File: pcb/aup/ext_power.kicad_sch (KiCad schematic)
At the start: 27 parts, among them Q1 AO3401A, Q2 AO3401A, U2 USBLC6-2SC6, U3 TPS563257DRLR

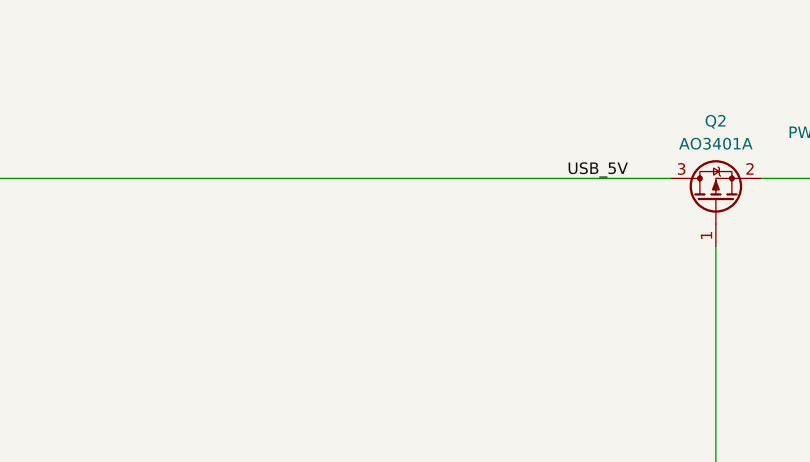
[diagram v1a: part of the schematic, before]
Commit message: Add some todo's on schematic. Add vias to fpga
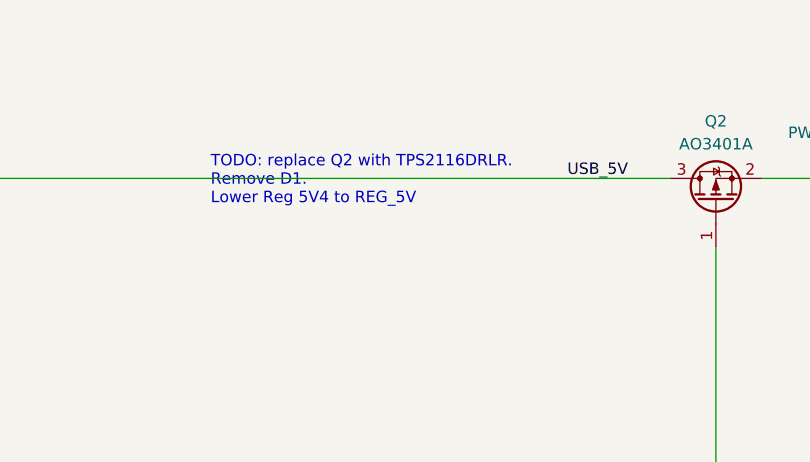
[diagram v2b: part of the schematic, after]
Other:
- note added: "TODO: replace Q2 with TPS2116DRLR. Remove D1. Lower Reg 5V4 to REG_5V"
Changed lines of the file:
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@@
 		(title "External Power")
+	)
+	(text "TODO: replace Q2 with TPS2116DRLR.\nRemove D1.\nLower Reg 5V4 to REG_5V"
+		(exclude_from_sim no)
+		(at 172.466 45.974 0)
+		(effects
+			(font
+				(size 1.27 1.27)
+			)
+			(justify left)
+		)
 	)
 	(text "The 12 to 5V regulator outputs 5.4V, with the expectation that it drops after \nthe Schottky by 0.3v under light load, and 0.5v under heavy load. (i.e. 4.9 to 5.1 final\nvoltages) This is based on the VF curves in the SS34 datasheet.\n\nR values based on availability of JLCPCB basic parts. The voltage divider for FB uses \nthe series resistors in the top portion since this seemed to be the only way to achieve\nthe desired ratio with basic parts."

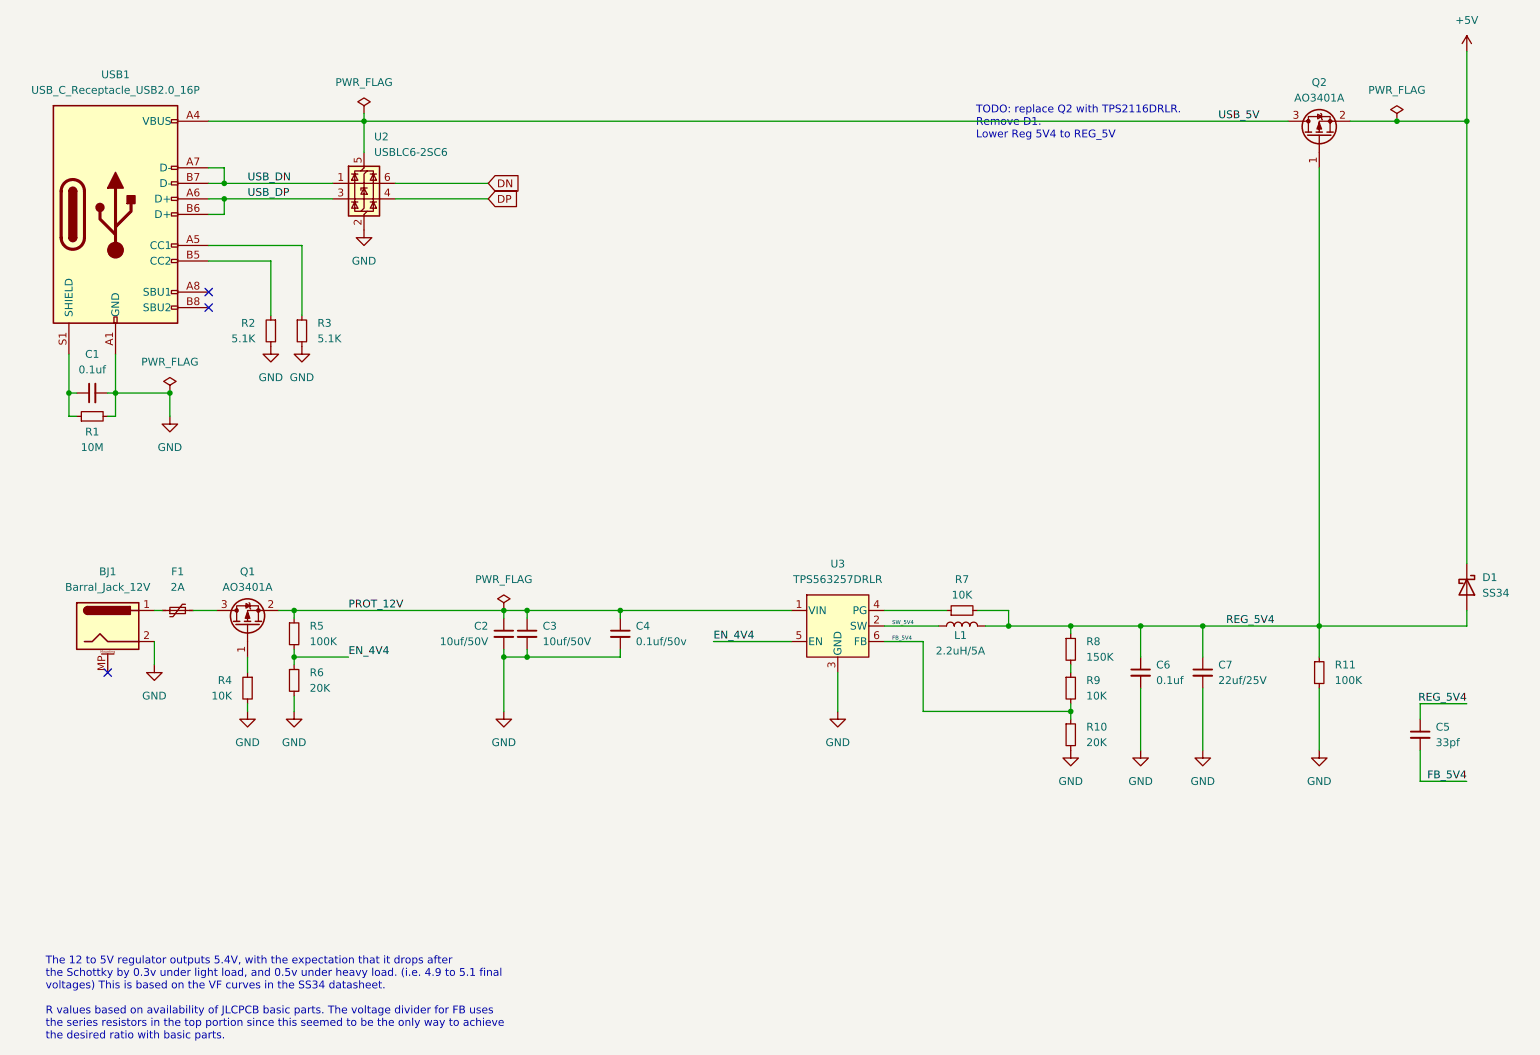
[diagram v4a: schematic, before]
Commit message: Use TPS2116DRLR for Vin mux
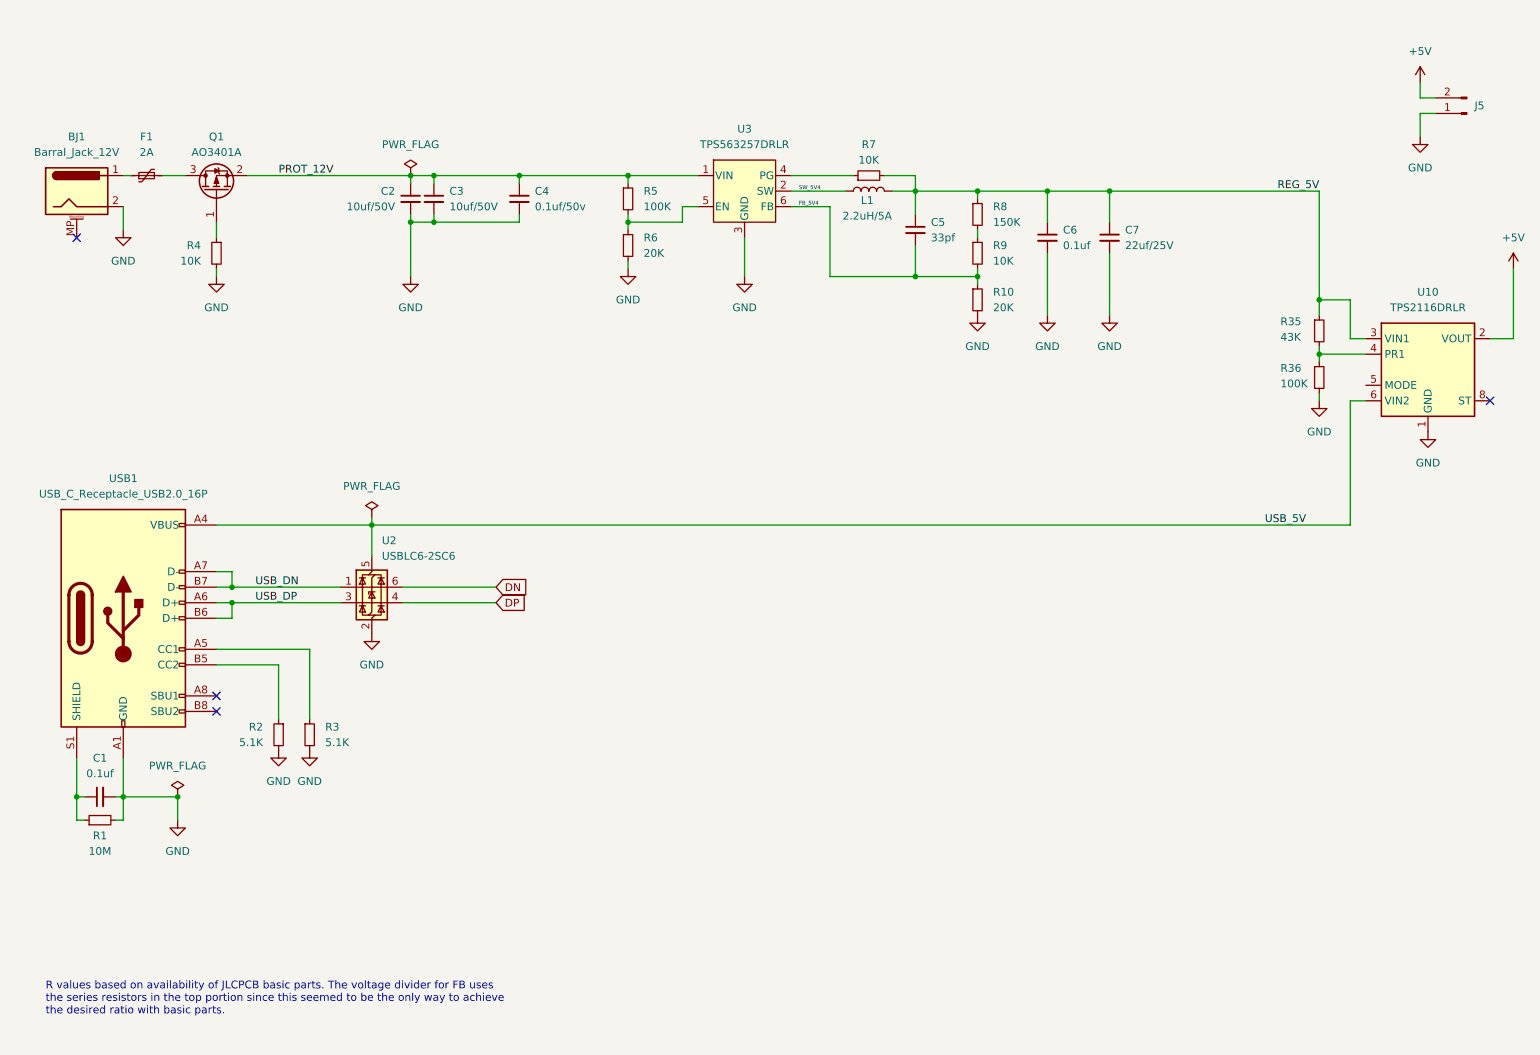
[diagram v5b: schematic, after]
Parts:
- removed D1: SS34, Diode_SMD:D_SMA, symbol !Misc:SS34
- removed Q2: AO3401A, Package_TO_SOT_SMD:SOT-23, symbol !Misc:AO3401A
- removed R11: 100K, Resistor_SMD:R_0603_1608Metric, symbol !Misc:R_100K_0603
- added J5: Conn_01x02_Pin, symbol Connector:Conn_01x02_Pin
- added R35: 43K, Resistor_SMD:R_0603_1608Metric, symbol !Misc:R_43K_0603
- added R36: 100K, Resistor_SMD:R_0603_1608Metric, symbol !Misc:R_100K_0603
- added U10: TPS2116DRLR, Package_TO_SOT_SMD:SOT-583-8, symbol !Misc:TPS2116DRLR
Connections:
- net +5V: now also J5.2 (Pin_2), U10.2 (VOUT), U10.7 (VOUT)
- net GND: now also J5.1 (Pin_1), R36.2, U10.1 (GND)
- net USB_5V: now also U10.6 (VIN2)
- net EN_4V4: no longer names the net of R5.2, R6.1, U3.5 (EN)
- net REG_5V4 renamed REG_5V
- net REG_5V: now also R35.1, U10.3 (VIN1)
- new net: R35.2, R36.1, U10.4 (PR1)
- no-connect marks 3 -> 4
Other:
- note added: "R values based on availability of JLCPCB basic parts. The voltage divider for FB uses the series resistors in the top portion since this seemed to be the only way to achieve the desired ratio with basic parts."
- note removed: "TODO: replace Q2 with TPS2116DRLR. Remove D1. Lower Reg 5V4 to REG_5V"
- note removed: "The 12 to 5V regulator outputs 5.4V, with the expectation that it drops after the Schottky by 0.3v under light load, and 0.5v under heavy load. (i.e. 4.9 to 5.1 final voltages) This is based on the VF curves in the SS34 datasheet. R values based on availability of JLCPCB basic parts. The voltage divider for FB uses the series resistors in the top portion since this seemed to be the only way to ac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"
- moved on the sheet: BJ1, C1, C2, C3, C4, C5, C6, C7, F1, L1, Q1, R1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

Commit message: Start of regulator rework
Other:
- moved on the sheet: U2
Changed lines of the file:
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@@
 	)
 	(junction
-		(at 73.66 111.76)
+		(at 80.01 111.76)
 		(diameter 0)
 		(color 0 0 0 0)
@@
 	(wire
 		(pts
-			(xy 73.66 111.76) (xy 73.66 116.84)
+			(xy 80.01 111.76) (xy 80.01 116.84)
 		)
 		(stroke
@@
 	(wire
 		(pts
-			(xy 48.26 111.76) (xy 73.66 111.76)
+			(xy 48.26 111.76) (xy 80.01 111.76)
 		)
 		(stroke
@@
 	(wire
 		(pts
-			(xy 73.66 111.76) (xy 73.66 110.49)
+			(xy 80.01 111.76) (xy 80.01 110.49)
 		)
 		(stroke
@@
 	(wire
 		(pts
-			(xy 50.8 124.46) (xy 68.58 124.46)
+			(xy 50.8 124.46) (xy 74.93 124.46)
 		)
 		(stroke
@@
 	(wire
 		(pts
-			(xy 78.74 124.46) (xy 93.98 124.46)
+			(xy 85.09 124.46) (xy 100.33 124.46)
 		)
 		(stroke
@@
 	(wire
 		(pts
-			(xy 50.8 121.92) (xy 68.58 121.92)
+			(xy 50.8 121.92) (xy 74.93 121.92)
 		)
 		(stroke
@@
 	(wire
 		(pts
+			(xy 80.01 111.76) (xy 233.68 111.76)
+		)
+		(stroke
+			(width 0)
+			(type default)
+		)
+	)
+	(wire
+		(pts
 			(xy 247.65 44.45) (xy 245.11 44.45)
 		)
@@
 	(wire
 		(pts
-			(xy 73.66 111.76) (xy 233.68 111.76)
-		)
-		(stroke
-			(width 0)
-			(type default)
-		)
-	)
-	(wire
-		(pts
 			(xy 31.75 156.21) (xy 33.02 156.21)
 		)
@@
 	(wire
 		(pts
-			(xy 78.74 121.92) (xy 93.98 121.92)
+			(xy 85.09 121.92) (xy 100.33 121.92)
 		)
 		(stroke
@@
 	(global_label "DP"
 		(shape input)
-		(at 93.98 124.46 0)
+		(at 100.33 124.46 0)
 		(fields_autoplaced yes)
 		(effects
@@
 		)
 		(property "Intersheetrefs" "${INTERSHEET_REFS}"
-			(at 99.5052 124.46 0)
+			(at 105.8552 124.46 0)
 			(effects
 				(font
@@
 	(global_label "DN"
 		(shape input)
-		(at 93.98 121.92 0)
+		(at 100.33 121.92 0)
 		(fields_autoplaced yes)
 		(effects
@@
 		)
 		(property "Intersheetrefs" "${INTERSHEET_REFS}"
-			(at 99.5657 121.92 0)
+			(at 105.9157 121.92 0)
 			(effects
 				(font
@@
 	(symbol
 		(lib_id "power:GND")
-		(at 73.66 129.54 0)
+		(at 80.01 129.54 0)
 		(unit 1)
 		(exclude_from_sim no)
@@
 		(fields_autoplaced yes)
 		(property "Reference" "#PWR06"
-			(at 73.66 135.89 0)
+			(at 80.01 135.89 0)
 			(effects
 				(font
@@
 		)
 		(property "Value" "GND"
-			(at 73.66 134.62 0)
+			(at 80.01 134.62 0)
 			(effects
 				(font
@@
 		)
 		(property "Footprint" ""
-			(at 73.66 129.54 0)
+			(at 80.01 129.54 0)
 			(effects
 				(font
@@
 		)
 		(property "Datasheet" ""
-			(at 73.66 129.54 0)
+			(at 80.01 129.54 0)
 			(effects
 				(font
@@
 		)
 		(property "Description" "Power symbol creates a global label with name \"GND\" , ground"
-			(at 73.66 129.54 0)
+			(at 80.01 129.54 0)
 			(effects
 				(font
@@
 	(symbol
 		(lib_id "!Misc:USBLC6-2SC6")
-		(at 73.66 121.92 0)
+		(at 80.01 121.92 0)
 		(unit 1)
 		(exclude_from_sim no)
@@
 		(fields_autoplaced yes)
 		(property "Reference" "U2"
-			(at 75.3111 114.3 0)
+			(at 81.6611 114.3 0)
 			(effects
 				(font
@@
 		)
 		(property "Value" "USBLC6-2SC6"
-			(at 75.3111 116.84 0)
+			(at 81.6611 116.84 0)
 			(effects
 				(font
@@
 		)
 		(property "Footprint" "Package_TO_SOT_SMD:SOT-23-6"
-			(at 74.93 128.27 0)
+			(at 81.28 128.27 0)
 			(effects
 				(font
@@
 		)
 		(property "Datasheet" "https://www.st.com/resource/en/datasheet/usblc6-2.pdf"
-			(at 74.93 130.175 0)
+			(at 81.28 130.175 0)
 			(effects
 				(font
@@
 		)
 		(property "Description" "Very low capacitance ESD protection diode, 2 data-line, SOT-23-6"
-			(at 73.66 121.92 0)
+			(at 80.01 121.92 0)
 			(effects
 				(font
@@
 		)
 		(property "LCSC Part #" "C7519"
-			(at 73.66 121.92 0)
+			(at 80.01 121.92 0)
 			(effects
 				(font
@@
 		)
 		(property "Digi-Key Part Number" "497-5235-1-ND"
-			(at 73.66 121.92 0)
+			(at 80.01 121.92 0)
 			(effects
 				(font
@@
 	(symbol
 		(lib_id "power:PWR_FLAG")
-		(at 73.66 110.49 0)
+		(at 80.01 110.49 0)
 		(unit 1)
 		(exclude_from_sim no)
@@
 		(dnp no)
 		(property "Reference" "#FLG02"
-			(at 73.66 108.585 0)
+			(at 80.01 108.585 0)
 			(effects
 				(font
@@
 		)
 		(property "Value" "PWR_FLAG"
-			(at 73.66 105.41 0)
+			(at 80.01 105.41 0)
 			(effects
 				(font
@@
 		)
 		(property "Footprint" ""
-			(at 73.66 110.49 0)
+			(at 80.01 110.49 0)
 			(effects
 				(font
@@
 		)
 		(property "Datasheet" "~"
-			(at 73.66 110.49 0)
+			(at 80.01 110.49 0)
 			(effects
 				(font
@@
 		)
 		(property "Description" "Special symbol for telling ERC where power comes from"
-			(at 73.66 110.49 0)
+			(at 80.01 110.49 0)
 			(effects
 				(font

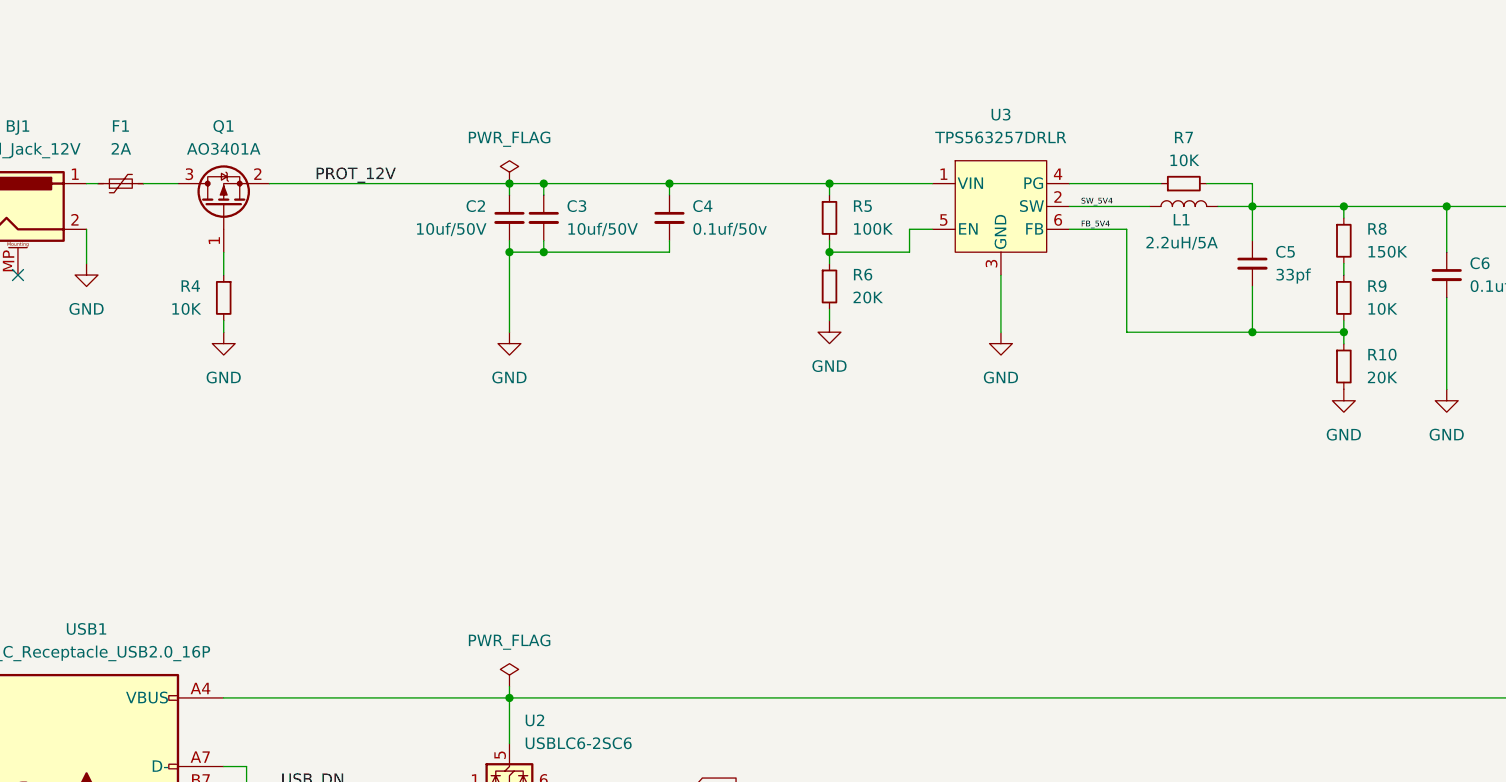
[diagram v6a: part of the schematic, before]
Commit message: Cleanup power layout
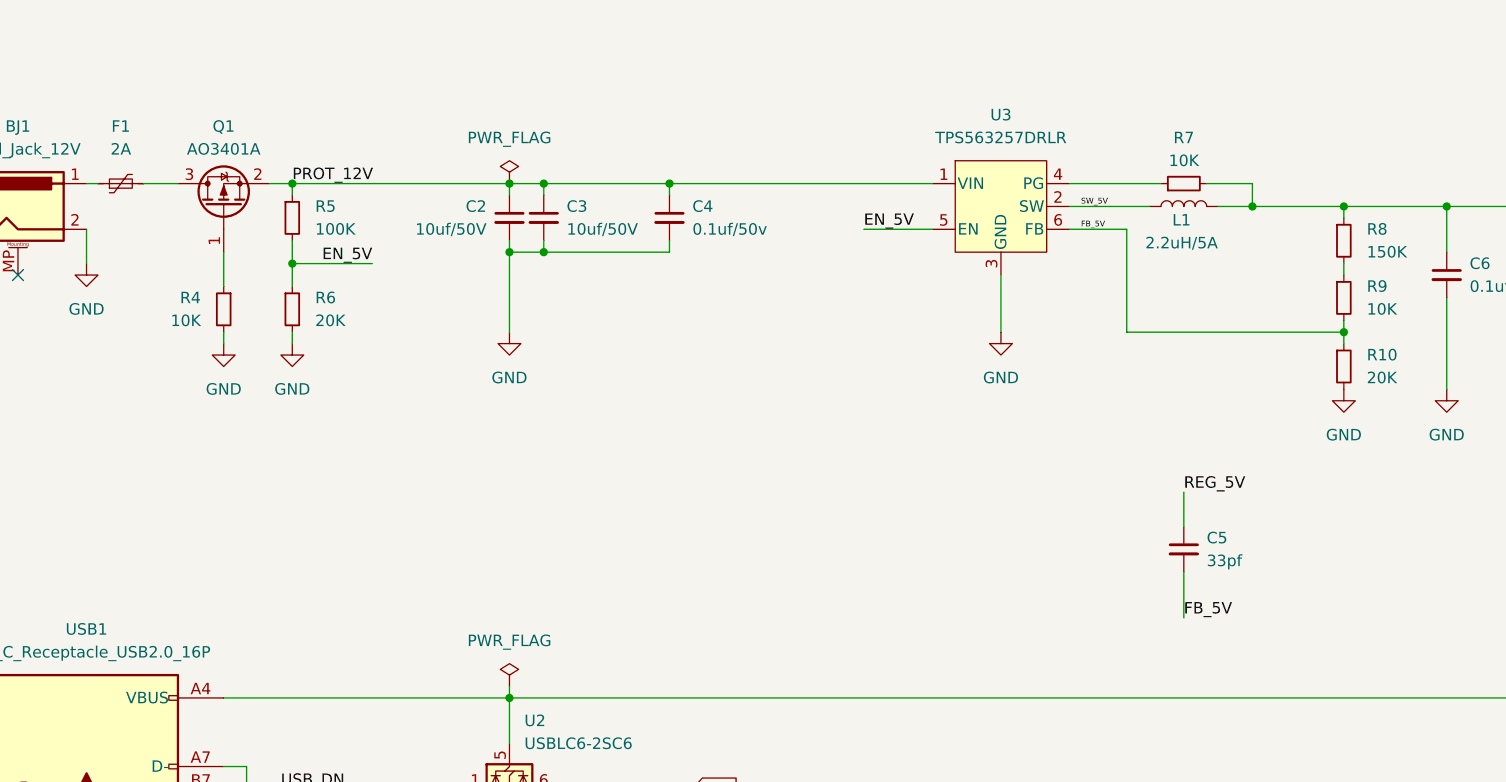
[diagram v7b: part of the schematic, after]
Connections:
- net EN_5V: now reaches R5.2, R6.1, U3.5 (EN)
- net FB_5V4 renamed FB_5V
- net SW_5V4 renamed SW_5V
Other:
- moved on the sheet: C5, R4, R5, R6

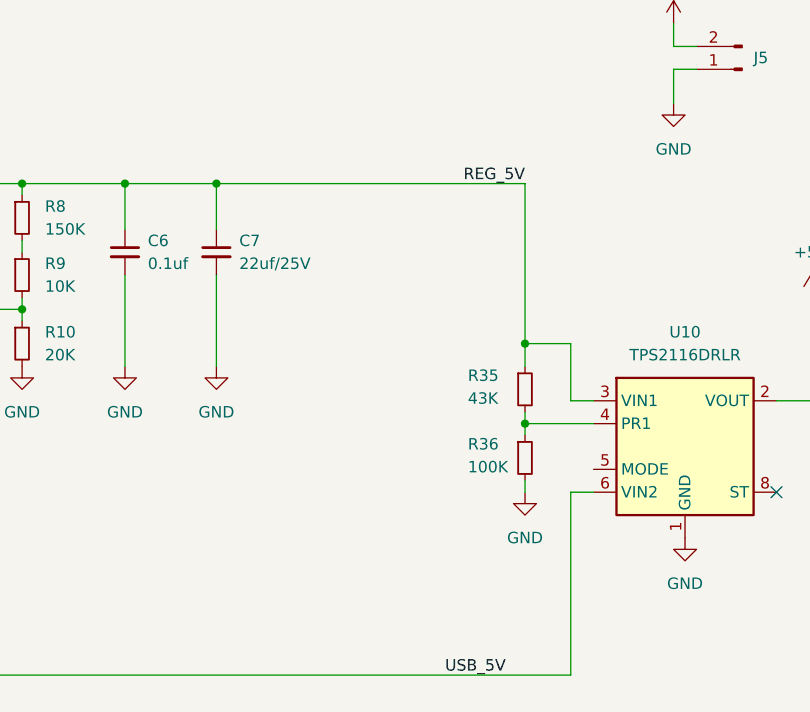
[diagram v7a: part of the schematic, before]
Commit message: All rails assigned net classes
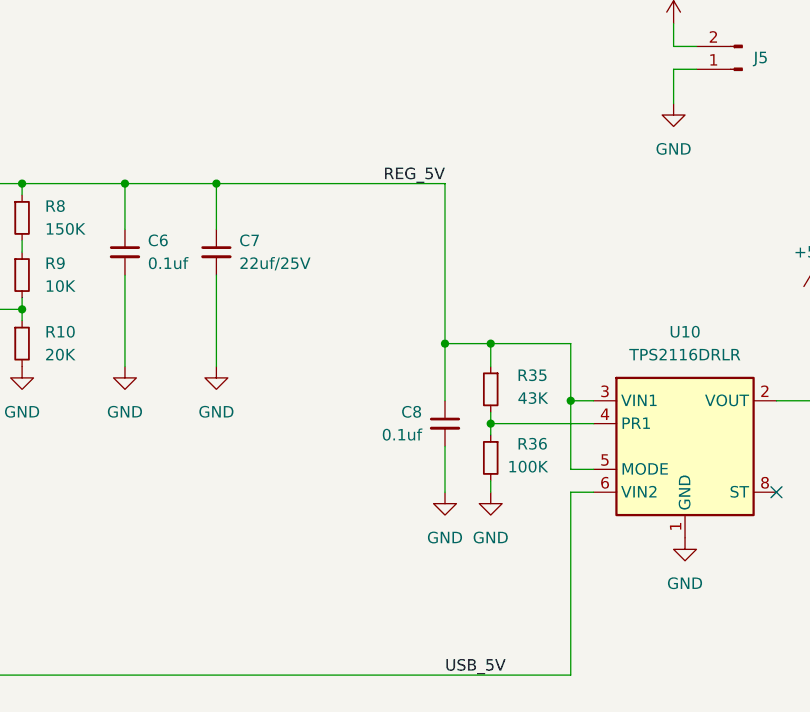
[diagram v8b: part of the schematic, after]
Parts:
- added C8: 0.1uf, Capacitor_SMD:C_0402_1005Metric, symbol !Misc:C_0.1uf_0402
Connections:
- net GND: now also C8.2
- net REG_5V: now also U10.5 (MODE), C8.1
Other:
- moved on the sheet: R35, R36
